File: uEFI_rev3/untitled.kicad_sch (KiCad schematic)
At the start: 31 parts, among them U36 MAX9926UAEE+

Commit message: uEFI rev 3.3
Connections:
- net +3V3: now also R60.1
- net CKP+: now also C41.1, D14.2 (A), JP11.3 (B)
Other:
- moved on the sheet: D14
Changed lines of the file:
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@@
   (junction (at 114.935 104.775) (diameter 1.016) (color 0 0 0 0)
+  )
+  (junction (at 86.995 37.465) (diameter 0) (color 0 0 0 0)
   )
   (junction (at 132.08 102.87) (diameter 1.016) (color 0 0 0 0)
@@
     (stroke (width 0) (type solid) (color 0 0 0 0))
   )
+  (wire (pts (xy 86.995 35.56) (xy 86.995 37.465))
+    (stroke (width 0) (type default) (color 0 0 0 0))
+  )
   (wire (pts (xy 106.045 107.95) (xy 106.045 104.775))
     (stroke (width 0) (type solid) (color 0 0 0 0))
   )
+  (wire (pts (xy 86.995 37.465) (xy 96.52 37.465))
+    (stroke (width 0) (type default) (color 0 0 0 0))
+  )
   (wire (pts (xy 124.46 100.33) (xy 124.46 125.095))
     (stroke (width 0) (type solid) (color 0 0 0 0))
@@
     (stroke (width 0) (type solid) (color 0 0 0 0))
   )
+  (wire (pts (xy 96.52 36.83) (xy 96.52 37.465))
+    (stroke (width 0) (type default) (color 0 0 0 0))
+  )
   (wire (pts (xy 171.45 115.57) (xy 171.45 119.38))
     (stroke (width 0) (type solid) (color 0 0 0 0))
@@
     (stroke (width 0) (type solid) (color 0 0 0 0))
   )
-  (wire (pts (xy 86.36 37.465) (xy 88.9 37.465))
+  (wire (pts (xy 83.82 37.465) (xy 86.995 37.465))
     (stroke (width 0) (type default) (color 0 0 0 0))
   )
@@
     (stroke (width 0) (type solid) (color 0 0 0 0))
   )
-  (wire (pts (xy 93.98 37.465) (xy 96.52 37.465))
-    (stroke (width 0) (type default) (color 0 0 0 0))
-  )
   (wire (pts (xy 108.585 41.275) (xy 108.585 44.45))
     (stroke (width 0) (type default) (color 0 0 0 0))
@@
     (stroke (width 0) (type solid) (color 0 0 0 0))
   )
+  (wire (pts (xy 86.995 29.21) (xy 86.995 30.48))
+    (stroke (width 0) (type default) (color 0 0 0 0))
+  )
   (wire (pts (xy 80.645 60.96) (xy 80.645 58.42))
     (stroke (width 0) (type solid) (color 0 0 0 0))
@@
   (wire (pts (xy 79.375 112.395) (xy 79.375 114.935))
     (stroke (width 0) (type solid) (color 0 0 0 0))
+  )
+  (wire (pts (xy 96.52 29.21) (xy 96.52 29.845))
+    (stroke (width 0) (type default) (color 0 0 0 0))
   )
   (wire (pts (xy 78.74 125.095) (xy 78.74 125.222))
@@
     )
   )
-  (global_label "CKP+" (shape input) (at 86.36 37.465 180)
+  (global_label "CKP+" (shape input) (at 83.82 37.465 180)
     (effects (font (size 1.27 1.27)) (justify right))
-    (property "Intersheet References" "${INTERSHEET_REFS}" (id 0) (at 78.5645 37.3856 0)
+    (property "Intersheet References" "${INTERSHEET_REFS}" (id 0) (at 76.0245 37.3856 0)
       (effects (font (size 1.27 1.27)) (justify right) hide)
     )
@@
     (pin "2")
   )
-  (symbol (lib_id "Device:R_Small") (at 91.44 37.465 270) (mirror x) (unit 1)
-    (in_bom yes) (on_board yes)
-    (property "Reference" "R60" (id 0) (at 91.44 35.56 90))
-    (property "Value" "10k" (id 1) (at 91.44 39.37 90))
-    (property "Footprint" "Resistor_SMD:R_0603_1608Metric" (id 2) (at 91.44 37.465 0)
-      (effects (font (size 1.27 1.27)) hide)
-    )
-    (property "Datasheet" "~" (id 3) (at 91.44 37.465 0)
+  (symbol (lib_id "Device:R_Small") (at 86.995 33.02 0) (mirror y) (unit 1)
+    (in_bom yes) (on_board yes)
+    (property "Reference" "R60" (id 0) (at 85.09 33.02 90))
+    (property "Value" "10k" (id 1) (at 88.9 33.02 90))
+    (property "Footprint" "Resistor_SMD:R_0603_1608Metric" (id 2) (at 86.995 33.02 0)
+      (effects (font (size 1.27 1.27)) hide)
+    )
+    (property "Datasheet" "~" (id 3) (at 86.995 33.02 0)
       (effects (font (size 1.27 1.27)) hide)
     )
@@
     (pin "2")
   )
+  (symbol (lib_id "power:+3V3") (at 86.995 29.21 0) (unit 1)
+    (in_bom yes) (on_board yes) (fields_autoplaced)
+    (property "Reference" "#PWR076" (id 0) (at 86.995 33.02 0)
+      (effects (font (size 1.27 1.27)) hide)
+    )
+    (property "Value" "+3V3" (id 1) (at 86.995 24.13 0))
+    (property "Footprint" "" (id 2) (at 86.995 29.21 0)
+      (effects (font (size 1.27 1.27)) hide)
+    )
+    (property "Datasheet" "" (id 3) (at 86.995 29.21 0)
+      (effects (font (size 1.27 1.27)) hide)
+    )
+    (pin "1")
+  )
   (symbol (lib_id "power:GND") (at 78.74 135.89 0) (unit 1)
     (in_bom yes) (on_board yes)
@@
     (pin "2")
   )
-  (symbol (lib_id "Diode:PMEG2020EH") (at 96.52 33.655 270) (unit 1)
+  (symbol (lib_id "Diode:PMEG2020EH") (at 96.52 33.02 270) (unit 1)
     (in_bom yes) (on_board yes) (fields_autoplaced)
-    (property "Reference" "D14" (id 0) (at 99.695 32.0674 90)
-      (effects (font (size 1.27 1.27)) (justify left))
-    )
-    (property "Value" "K26" (id 1) (at 99.695 34.6074 90)
+    (property "Reference" "D14" (id 0) (at 99.695 31.4324 90)
+      (effects (font (size 1.27 1.27)) (justify left))
+    )
+    (property "Value" "K26" (id 1) (at 99.695 33.9724 90)
       (effects (font (size 1.27 1.27)) (justify left) hide)
     )
-    (property "Footprint" "Diode_SMD:D_SOD-123F" (id 2) (at 92.075 33.655 0)
-      (effects (font (size 1.27 1.27)) hide)
-    )
-    (property "Datasheet" "https://datasheet.lcsc.com/lcsc/2111221830_GOODWORK-K26_C2922179.pdf" (id 3) (at 96.52 33.655 0)
-      (effects (font (size 1.27 1.27)) hide)
-    )
-    (property "LCSC" "C2922179" (id 4) (at 96.52 33.655 90)
+    (property "Footprint" "Diode_SMD:D_SOD-123F" (id 2) (at 92.075 33.02 0)
+      (effects (font (size 1.27 1.27)) hide)
+    )
+    (property "Datasheet" "https://datasheet.lcsc.com/lcsc/2111221830_GOODWORK-K26_C2922179.pdf" (id 3) (at 96.52 33.02 0)
+      (effects (font (size 1.27 1.27)) hide)
+    )
+    (property "LCSC" "C2922179" (id 4) (at 96.52 33.02 90)
       (effects (font (size 0.889 0.889)) hide)
     )

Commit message: pre-production files, uEFI v3.4
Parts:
- D14: footprint Diode_SMD:D_SOD-123F -> Diode_SMD:D_SOD-323; symbol Diode:PMEG2020EH -> Diode:BAS316
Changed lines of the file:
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@@
     (pin "2")
   )
-  (symbol (lib_id "Diode:PMEG2020EH") (at 96.52 33.02 270) (unit 1)
+  (symbol (lib_id "Diode:BAS316") (at 96.52 33.02 270) (unit 1)
     (in_bom yes) (on_board yes) (fields_autoplaced)
     (property "Reference" "D14" (id 0) (at 99.695 31.4324 90)
@@
       (effects (font (size 1.27 1.27)) (justify left) hide)
     )
-    (property "Footprint" "Diode_SMD:D_SOD-123F" (id 2) (at 92.075 33.02 0)
+    (property "Footprint" "Diode_SMD:D_SOD-323" (id 2) (at 92.075 33.02 0)
       (effects (font (size 1.27 1.27)) hide)
     )
-    (property "Datasheet" "https://datasheet.lcsc.com/lcsc/2111221830_GOODWORK-K26_C2922179.pdf" (id 3) (at 96.52 33.02 0)
+    (property "Datasheet" "https://assets.nexperia.com/documents/data-sheet/BAS16_SER.pdf" (id 3) (at 96.52 33.02 0)
       (effects (font (size 1.27 1.27)) hide)
     )

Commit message: fix bom output
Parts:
- R121, R122: value R_Small -> 10k
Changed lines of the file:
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@@
       (effects (font (size 1.27 1.27)) (justify left))
     )
-    (property "Value" "R_Small" (id 1) (at 181.8387 81.1593 0)
+    (property "Value" "10k" (id 1) (at 181.8387 81.1593 0)
       (effects (font (size 1.27 1.27)) (justify left))
     )
@@
       (effects (font (size 1.27 1.27)) (justify left))
     )
-    (property "Value" "R_Small" (id 1) (at 193.2687 83.6993 0)
+    (property "Value" "10k" (id 1) (at 193.2687 83.6993 0)
       (effects (font (size 1.27 1.27)) (justify left))
     )

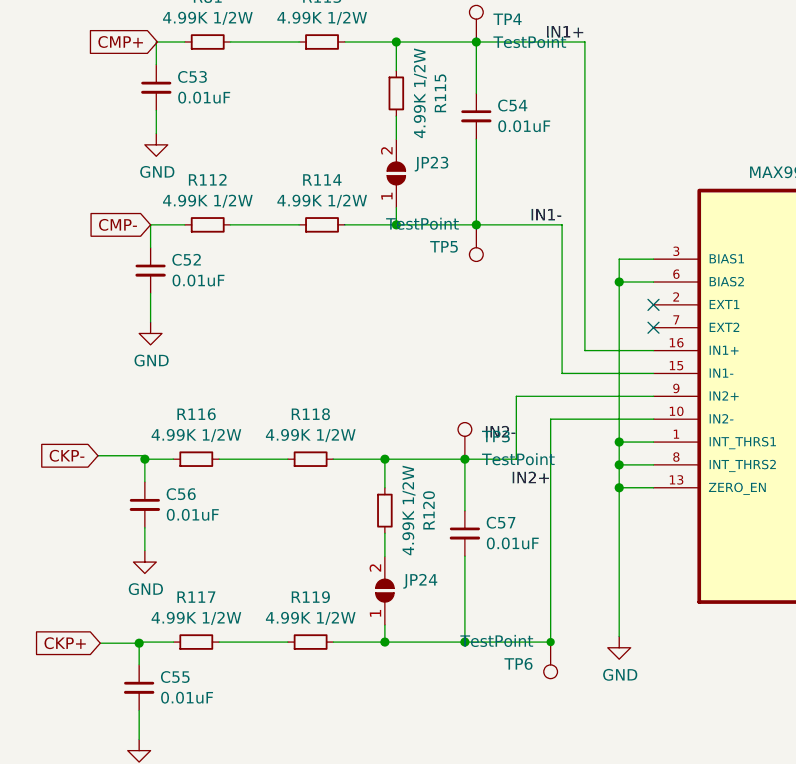
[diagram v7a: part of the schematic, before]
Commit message: uEFI v3, fix 12v => 5v overcurrent issue
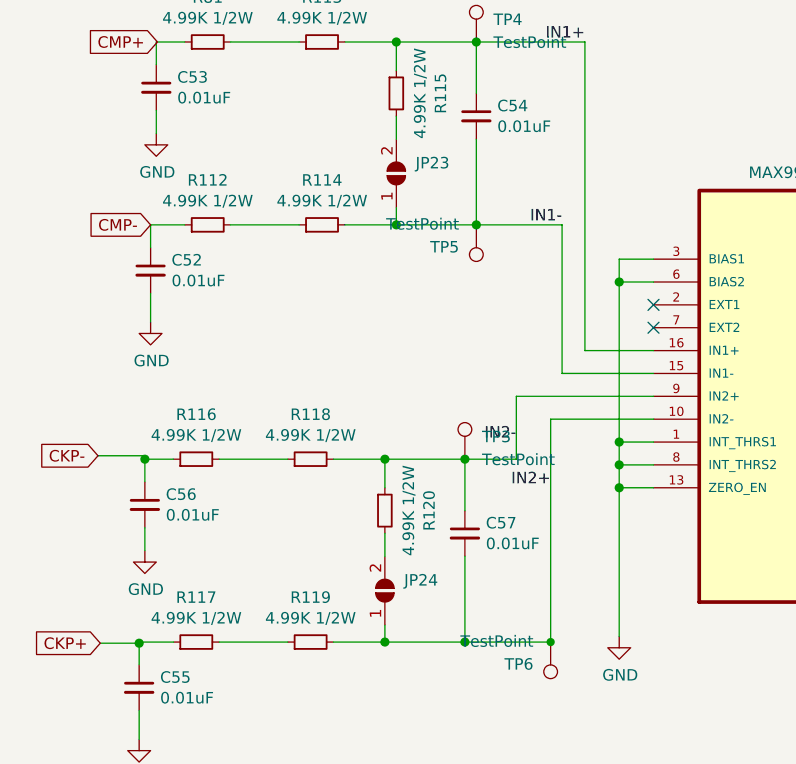
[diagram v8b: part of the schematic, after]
